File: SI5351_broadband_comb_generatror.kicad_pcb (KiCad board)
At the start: 4 copper layers, 150 x 75 mm, 119 parts, among them J1 Conn_Coaxial_Small, J10 Conn_01x06_Socket, J11 RFShield_TwoPieces, J2 RFShield_TwoPieces, J3 Barrel_Jack_Switch, J4 Conn_Coaxial_Small, J5 Conn_01x10_Pin, J6 Conn_01x06_Socket, J7 USB_B, J8 AVR-ISP-6, J9 Conn_Coaxial_Small, SW1 SW_SP5T_NR01105, U1 ISL3280ExHZ, U10 ATmega328PB-A, U11 FT232RL, U12 WE-TVS-82400102, U13 PAT1220-C-3DB, U2 PHA-13HLN+, U4 KT2520K-T, U5 Si5351C-B-GM, U6 PHA-13HLN+, U7 PAT1220-C-3DB, U8 AMS1117-3.3, U9 L7809, Y1 ECS-2520MV-xxx-xx

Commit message: noch ein paar Kleinigkeiten
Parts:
- added C14: 100n, Capacitor_SMD:C_0805_2012Metric_Pad1.18x1.45mm_HandSolder, B.Cu at (130.2, 86.4)
- added C51: 100n, Capacitor_SMD:C_0805_2012Metric_Pad1.18x1.45mm_HandSolder, B.Cu at (130.2, 84.4)
- added C52: 100n, Capacitor_SMD:C_0805_2012Metric_Pad1.18x1.45mm_HandSolder, B.Cu at (130.2, 82.4)
- added C53: 100n, Capacitor_SMD:C_0805_2012Metric_Pad1.18x1.45mm_HandSolder, B.Cu at (137.0, 79.4)
- added C54: 100n, Capacitor_SMD:C_0805_2012Metric_Pad1.18x1.45mm_HandSolder, B.Cu at (139.1, 79.4)
- moved J10 7.50 mm to (224.5, 81.1)
- moved SW1 7.50 mm to (231.5, 82.4)
- moved J6 2.20 mm to (204.8, 81.2)
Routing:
- net Net-(J10-Pin_3): track 113.0 -> 107.5 mm
- net Net-(J10-Pin_4): track 117.5 -> 113.7 mm
- net Net-(J10-Pin_2): track 109.8 -> 106.2 mm
- net Net-(J10-Pin_5): track 112.5 -> 109.1 mm
- net Net-(J10-Pin_1): track 99.4 -> 96.5 mm
- net Net-(J10-Pin_6): track 134.2 -> 132.7 mm
- net GND: vias 781 -> 780
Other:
- board size 150 x 75 mm -> 142 x 75 mm

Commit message: BOM angefangen und im Layout vom Hundertsten ins Tausendste gekommen...
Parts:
- removed U4: KT2520K-T, Oscillator:Oscillator_SMD_Kyocera_2520-6Pin_2.5x2.0mm
- added Y2: TG2520SMN-xx.xxxxxxMhz-xxxxNM, Oscillator:Oscillator_SMD_SeikoEpson_TG2520SMN-xxx-xxxxxx-4Pin_2.5x2.0mm, F.Cu at (152.4, 84.9)
- RV1, RV2: footprint Potentiometer_SMD:Potentiometer_Bourns_3214J_Horizontal -> Potentiometer_SMD:Potentiometer_Bourns_TC33X_Vertical
- moved C6 1.58 mm to (176.6, 69.9), turned to -90 degrees
- moved R12 1.57 mm to (178.6, 69.9), turned to 90 degrees
- moved RV1 1.13 mm to (182.2, 69.9), turned to 0 degrees
- moved R8 0.53 mm to (177.8, 115.6), turned to 90 degrees
- moved C47 0.53 mm to (175.8, 115.6), turned to -90 degrees
- moved RV2 0.43 mm to (182.0, 115.6), turned to 0 degrees
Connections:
- SW1 pad 1: Net-(J10-Pin_6) -> Net-(J10-Pin_3)
- SW1 pad 3: Net-(J10-Pin_4) -> Net-(J10-Pin_6)
- SW1 pad 4: Net-(J10-Pin_3) -> Net-(J10-Pin_4)
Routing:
- net Net-(J10-Pin_6): track 132.7 -> 115.5 mm
- net Net-(J10-Pin_3): track 107.5 -> 101.6 mm
- net GND: track 113.3 -> 107.9 mm, vias 780 -> 772
- net Net-(C26-Pad1): track 28.6 -> 23.5 mm
- net Net-(C35-Pad1): track 29.0 -> 23.9 mm
- net Net-(J10-Pin_4): track 113.7 -> 116.2 mm
- net /Comb_Generator/INTR: track 22.0 -> 19.5 mm
- net /Comb_Generator/3V3D: track 33.9 -> 35.0 mm
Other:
- board text added: "+3.3V"
- board text added: "+9-14V DC"
- board text added: "+9V"
- board text added: "10 MHz EXT Ref."
- board text added: "AVR ISP"
- board text added: "SI5351 Kammgenerator Professur für TET und EMV, TU Dresden 2025 DM2LCT"

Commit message: es wird nicht besser... Beschriftungen und co. BOM angefangen...
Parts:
- added D5: LED_Small, LED_SMD:LED_0805_2012Metric_Pad1.15x1.40mm_HandSolder, F.Cu at (152.0, 110.0)
- added D7: LED_Small, LED_SMD:LED_0805_2012Metric_Pad1.15x1.40mm_HandSolder, F.Cu at (149.0, 110.0)
- added R11: 1k, Resistor_SMD:R_0805_2012Metric_Pad1.20x1.40mm_HandSolder, F.Cu at (152.0, 114.0)
- added R16: 1k, Resistor_SMD:R_0805_2012Metric_Pad1.20x1.40mm_HandSolder, F.Cu at (149.0, 114.0)
- added REF**: OSHW-Logo_7.5x8mm_SolderMask, Symbol:OSHW-Logo_7.5x8mm_SolderMask, F.Cu at (182.5, 88.5)
- moved C25 0.30 mm to (176.6, 66.0)
- moved C7 0.30 mm to (173.7, 65.1)
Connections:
- U11 pad 22: unconnected-(U11-CBUS1-Pad22) -> Net-(U11-CBUS1)
- U11 pad 23: unconnected-(U11-CBUS0-Pad23) -> Net-(U11-CBUS0)
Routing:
- net Net-(U11-CBUS0): track 0.00 -> 18.1 mm
- net Net-(U11-CBUS1): track 0.00 -> 15.5 mm
- net Net-(D7-A): track 0.00 -> 1.97 mm
- net Net-(D5-A): track 0.00 -> 1.97 mm
- net GND: track 107.9 -> 107.0 mm, vias 772 -> 781
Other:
- board text added: "RX"
- board text added: "TX"

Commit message: Maybe ready for production...
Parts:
- FL2: footprint Inductor_SMD:L_CommonMode_Wuerth_WE-SL2 -> Inductor_SMD:L_CommonMode_Wuerth_WE-SL2_alt
- U9: footprint Package_TO_SOT_SMD:TO-252-3_TabPin2 -> Package_TO_SOT_SMD:TO-252-2
- moved U9 0.14 mm to (143.9, 61.5)
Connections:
- FL2 pad 2: /Power_Supply/VIN- -> Net-(D4-A2)
- FL2 pad 3: Net-(D4-A1) -> /Power_Supply/VIN-
- FL2 pad 4: Net-(D4-A2) -> Net-(D4-A1)
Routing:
- net +3V3: track 80.7 -> 79.8 mm, vias 4 -> 35
- net Net-(J10-Pin_1): track 96.7 -> 97.3 mm
- net GND: vias 781 -> 803
- added copper zone on F.Cu, net +3V3
- added copper zone on In2.Cu, net +3V3

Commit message: Maybe now... ready for production...
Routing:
- net GND: track 107.0 -> 116.6 mm, vias 803 -> 835

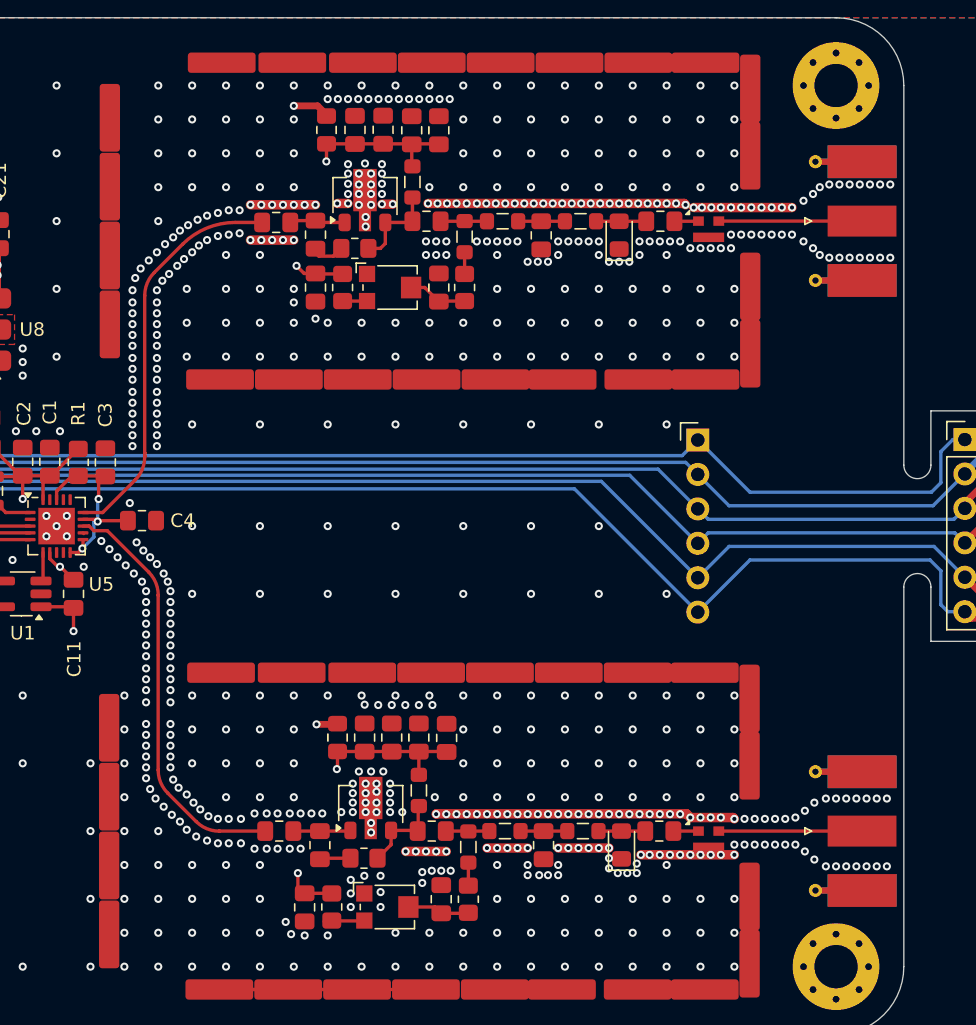
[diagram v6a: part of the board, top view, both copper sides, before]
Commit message: got samples von Minicircuits, change attenuator to GAT-x
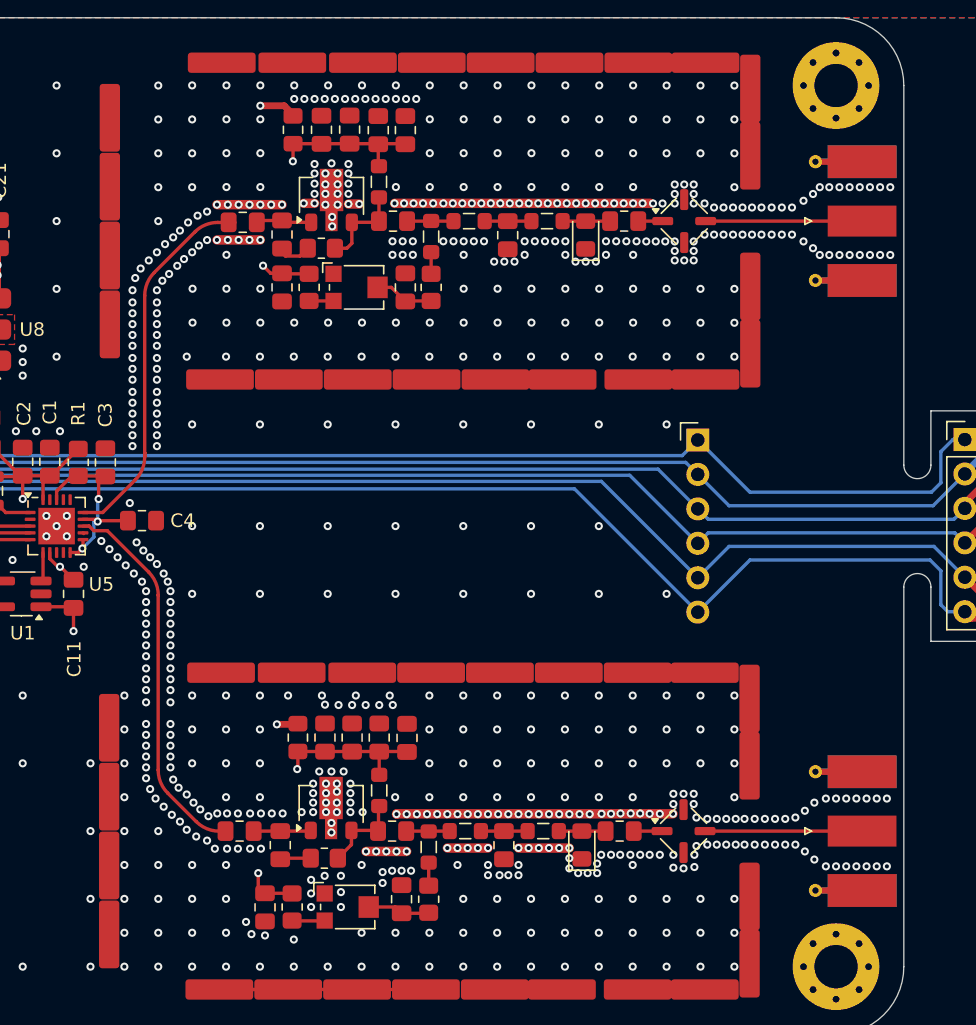
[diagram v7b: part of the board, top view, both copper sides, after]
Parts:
- removed U13, U7: PAT1220-C-3DB, RF_Converter:RF_Attenuator_Susumu_PAT1220
- added U3: GAT-10+, Package_DFN_QFN:Mini-Circuits_FG873-4_3x3mm, F.Cu at (203.8, 65.0)
- added U4: GAT-10+, Package_DFN_QFN:Mini-Circuits_FG873-4_3x3mm, F.Cu at (203.8, 110.0)
- moved C27 2.93 mm to (171.0, 110.0)
- moved C33 2.93 mm to (174.0, 111.0)
- moved C34 2.93 mm to (182.2, 110.0)
- moved C36 2.93 mm to (182.9, 115.0)
- moved C41 2.93 mm to (190.5, 111.0)
- moved C43 2.93 mm to (199.0, 110.0)
- moved C47 2.93 mm to (172.9, 115.6)
- moved C48 2.93 mm to (183.3, 103.1)
- moved D3 2.93 mm to (196.2, 111.0)
- moved L6 2.93 mm to (184.9, 111.2)
- moved R4 2.93 mm to (177.2, 112.0)
- moved R7 2.93 mm to (184.9, 115.0)
- moved R8 2.93 mm to (174.9, 115.6)
- moved RV2 2.93 mm to (179.1, 115.6)
- moved U2 2.93 mm to (177.8, 108.0)
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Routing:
- net GND: track 116.6 -> 100.6 mm, vias 835 -> 844
- net +9VA: track 95.0 -> 89.6 mm
- net /Comb_Generator/CLK0: track 31.1 -> 28.2 mm
- net /Comb_Generator/CLK1: track 29.7 -> 27.9 mm
- net /Comb_Generator/comb_out_2: track 10.6 -> 11.6 mm
- net /Comb_Generator/comb_out_1: track 10.6 -> 11.6 mm
